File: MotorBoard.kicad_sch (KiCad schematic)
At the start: 34 parts

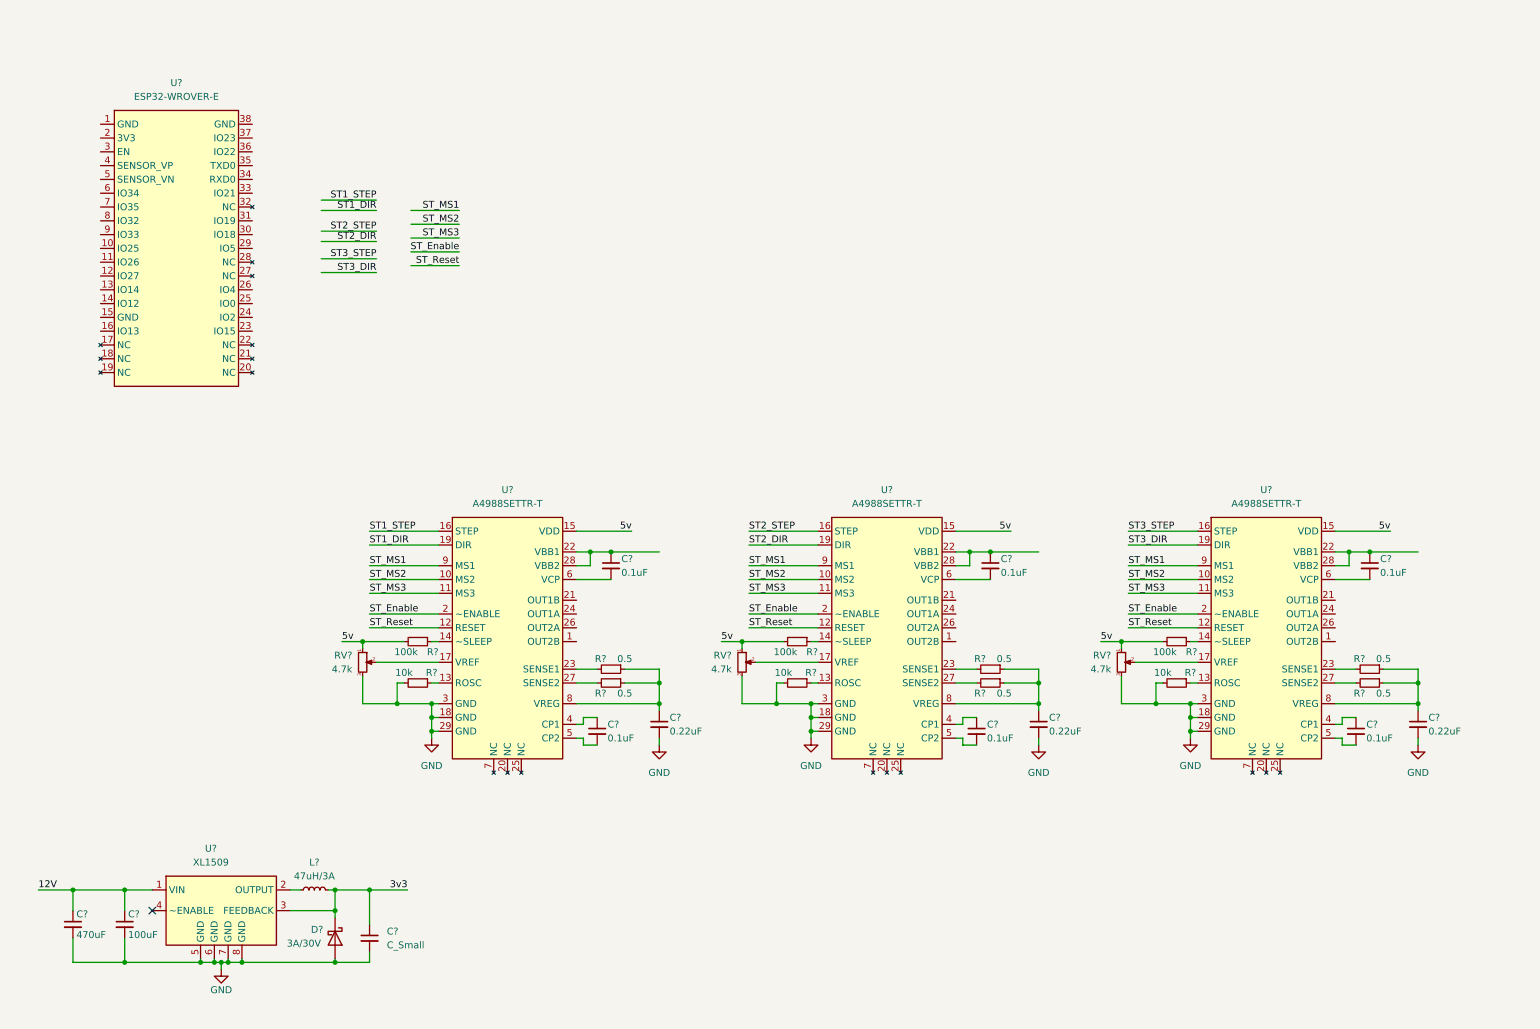
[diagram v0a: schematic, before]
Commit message: Wired stepper driver and power supply section
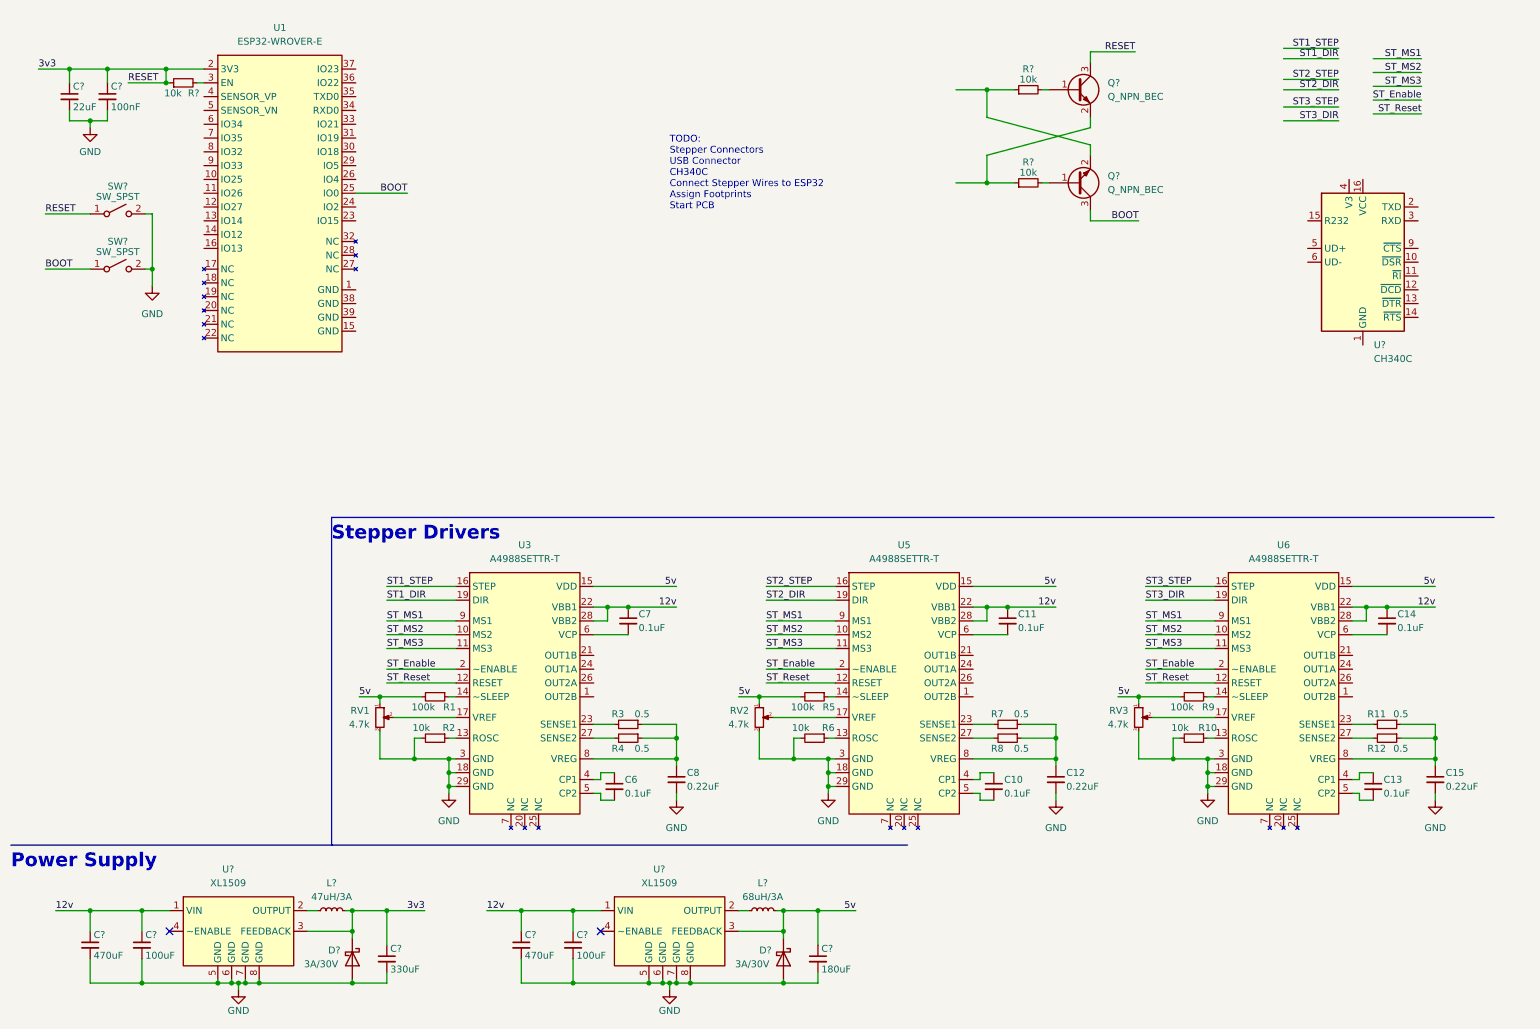
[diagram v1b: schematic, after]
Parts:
- removed C?: C_Small, symbol Device:C_Small
- removed C?: 100uF, symbol Device:C_Small
- removed C?: 470uF, symbol Device:C_Small
- removed D?: 3A/30V, symbol Device:D_Schottky
- removed L?: 47uH/3A, symbol Device:L_Small
- removed U?: XL1509, symbol MotorBoard:XL1509
- added C? (x2): 100uF, symbol Device:C_Small
- added C? (x2): 470uF, symbol Device:C_Small
- added C?: 330uF, symbol Device:C_Small
- added C?: 180uF, symbol Device:C_Small
- added C?: 100nF, symbol Device:C_Small
- added C?: 22uF, symbol Device:C_Small
- added D? (x2): 3A/30V, symbol Device:D_Schottky
- added L?: 47uH/3A, symbol Device:L_Small
- added L?: 68uH/3A, symbol Device:L_Small
- added Q? (x2): Q_NPN_BEC, symbol Device:Q_NPN_BEC
- added R? (x3): 10k, symbol Device:R_Small
- added SW? (x2): SW_SPST, symbol Switch:SW_SPST
- added U?: CH340C, Package_SO:SOIC-16_3.9x9.9mm_P1.27mm, symbol Interface_USB:CH340C
- added U? (x2): XL1509, symbol MotorBoard:XL1509
- U1: renamed from U?; LSCS Part Number (none) -> C2934565
- U3, U5, U6: renamed from U?; LSCS Part Number (none) -> C38437
- gave numbers to parts that had none: 24
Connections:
- net 3v3: now also U1.2 (3V3), C?.1, C?.1, C?.1, D?.1 (K), L?.2, Q?.3 (C), R?.1, SW?.1 (A), U?.3 (FEEDBACK)
- net 5v: now also C?.1, D?.1 (K), L?.2, U?.3 (FEEDBACK)
- net GND: now also C?.2, C?.2, C?.2, C?.2, C?.2, C?.2, C?.2, C?.2, D?.2 (A), D?.2 (A), SW?.2 (B), SW?.2 (B), U?.5 (GND), U?.5 (GND), U?.6 (GND), U?.6 (GND), U?.7 (GND), U?.7 (GND), U?.8 (GND), U?.8 (GND)
- net 12v: now reaches C14.1, U6.22 (VBB1), U6.28 (VBB2)
- net 12v: now also C11.1, C7.1, U3.22 (VBB1), U3.28 (VBB2), U5.22 (VBB1), U5.28 (VBB2), C?.1, C?.1, C?.1, C?.1, U?.1 (VIN), U?.1 (VIN)
- net BOOT: now reaches U1.25 (IO0)
- net BOOT: now also Q?.3 (C), SW?.1 (A)
- net at U1.3 (EN): now also R?.2
- new net: L?.1, U?.2 (OUTPUT) (x2)
- new net: Q?.1 (B), R?.2 (x2)
- new net: Q?.2 (E), R?.1 (x2)
- no-connect marks 1 -> 2
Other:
- note added: "Power Supply"
- note added: "Stepper Drivers"
- note added: "TODO: Stepper Connectors USB Connector CH340C Connect Stepper Wires to ESP32 Assign Footprints Start PCB"
- moved on the sheet: C10, C11, C12, C13, C14, C15, C6, C7, C8, R1, R10, R11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

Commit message: Broke stepper drivers into hierarchial sheets
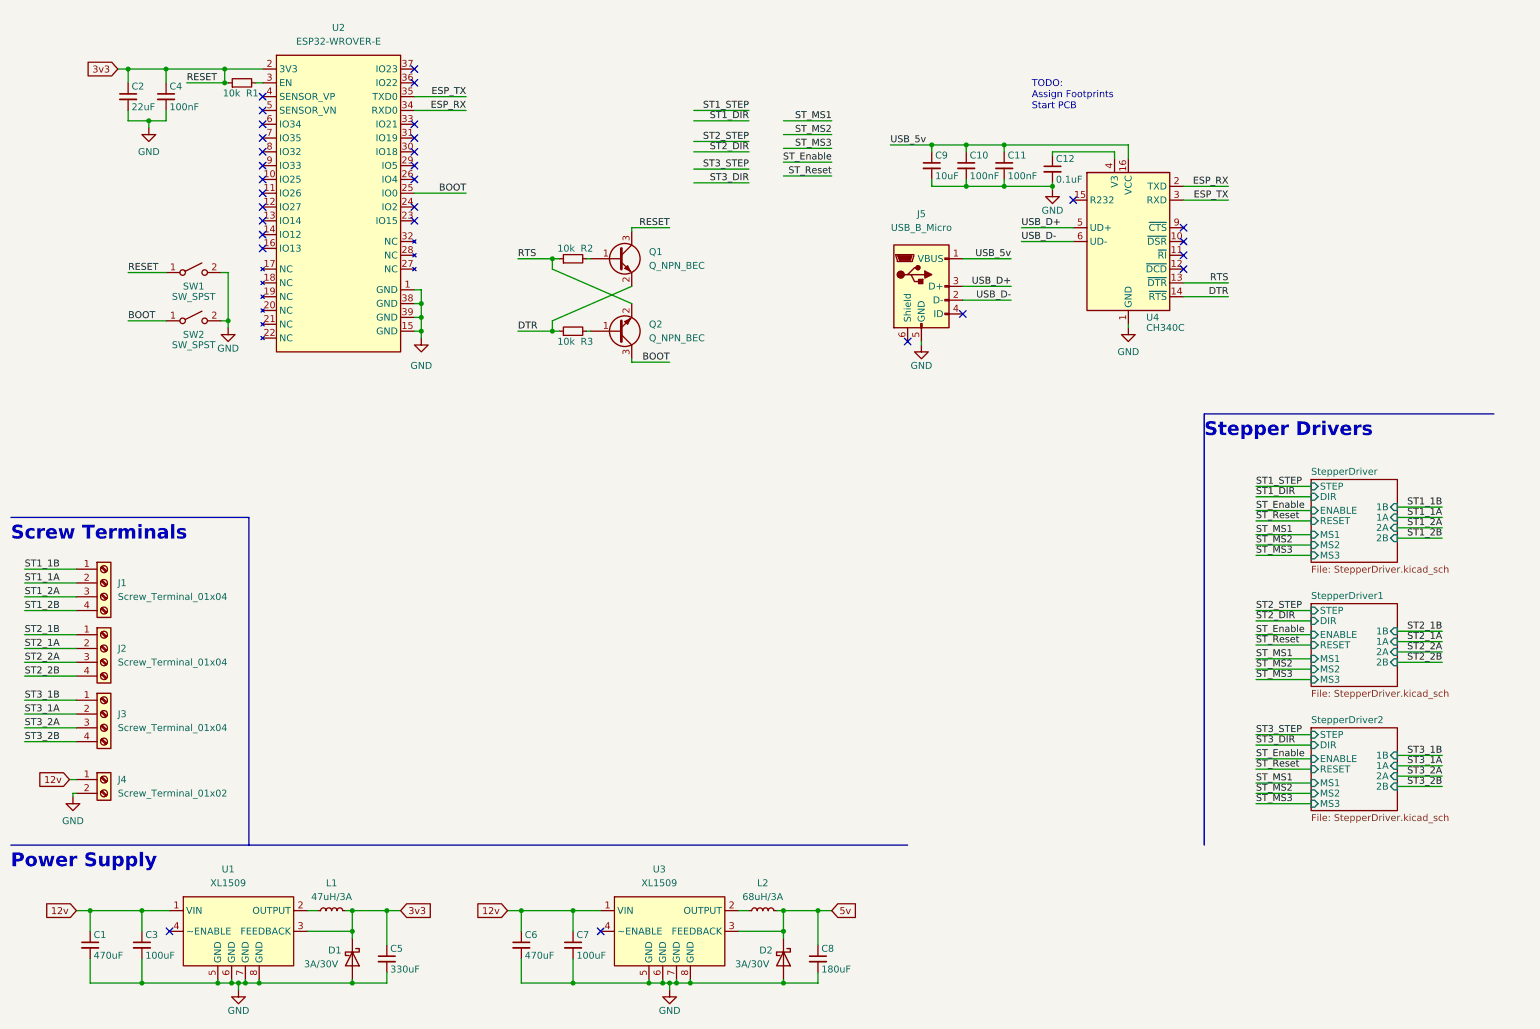
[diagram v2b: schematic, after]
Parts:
- removed C13, C14, C6, C7: 0.1uF, symbol Device:C_Small
- removed C15, C8: 0.22uF, symbol Device:C_Small
- removed R1, R5, R9: 100k, symbol Device:R_Small
- removed R10, R2, R6: 10k, symbol Device:R_Small
- removed R11, R12, R3, R4, R7, R8: 0.5, symbol Device:R_Small
- removed RV1, RV2, RV3: 4.7k, symbol Device:R_Potentiometer_Small
- removed U3, U5, U6: A4988SETTR-T, symbol MotorBoard:A4988SETTR-T
- added C9: 10uF, symbol Device:C_Small
- added J1, J2, J3: Screw_Terminal_01x04, symbol Connector:Screw_Terminal_01x04
- added J4: Screw_Terminal_01x02, symbol Connector:Screw_Terminal_01x02
- added J5: USB_B_Micro, symbol Connector:USB_B_Micro
- C10, C11: value 0.1uF -> 100nF
- C12: value 0.22uF -> 0.1uF
- gave numbers to parts that had none: 22
- renumbered U1 to U2
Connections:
- net 12v: now also J4.1 (Pin_1); no longer C11.1
- net GND: now also C10.2, C11.2, U2.1 (GND), U2.15 (GND), U2.38 (GND), U2.39 (GND), U4.1 (GND), C9.2, J4.2 (Pin_2), J5.5 (GND)
- net RTS: now reaches U4.13 (~{DTR})
- net RTS: now also Q2.2 (E), R2.1
- net DTR: now reaches U4.14 (~{RTS})
- net DTR: now also Q1.2 (E), R3.1
- net USB_5v: now reaches U4.16 (VCC)
- net USB_5v: now also C10.1, C11.1, C9.1, J5.1 (VBUS)
- net ESP_RX: now reaches U4.2 (TXD)
- net ESP_RX: now also U2.34 (RXD0)
- net ESP_TX: now reaches U4.3 (RXD)
- net ESP_TX: now also U2.35 (TXD0)
- net at U4.4 (V3): now also C12.1
- net USB_D+: now reaches U4.5 (UD+)
- net USB_D+: now also J5.3 (D+)
- net USB_D-: now reaches U4.6 (UD-)
- net USB_D-: now also J5.2 (D-)
- new net ST1_1A: J1.2 (Pin_2)
- new net ST1_1B: J1.1 (Pin_1)
- new net ST1_2A: J1.3 (Pin_3)
- new net ST1_2B: J1.4 (Pin_4)
- new net ST2_1A: J2.2 (Pin_2)
- new net ST2_1B: J2.1 (Pin_1)
- new net ST2_2A: J2.3 (Pin_3)
- new net ST2_2B: J2.4 (Pin_4)
- new net ST3_1A: J3.2 (Pin_2)
- new net ST3_1B: J3.1 (Pin_1)
- new net ST3_2A: J3.3 (Pin_3)
- new net ST3_2B: J3.4 (Pin_4)
- no-connect marks 2 -> 30
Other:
- added sheet StepperDriver (StepperDriver.kicad_sch)
- added sheet StepperDriver1 (StepperDriver.kicad_sch)
- added sheet StepperDriver2 (StepperDriver.kicad_sch)
- note added: "Screw Terminals"
- note added: "TODO: Assign Footprints Start PCB"
- note removed: "TODO: Stepper Connectors USB Connector CH340C Connect Stepper Wires to ESP32 Assign Footprints Start PCB"
- moved on the sheet: C2, C4, Q1, Q2, R1, R2, R3, SW1, SW2, U2, U4

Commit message: Added part numbers to majority of components
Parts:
- C1, C3, C5, C6, C7, C8: footprint (none) -> Capacitor_SMD:C_0603_1608Metric
- C10, C11, C4: footprint (none) -> Capacitor_SMD:C_0603_1608Metric; LSCS Part Number (none) -> C1591; Manufacturer Part Number (none) -> CL10B104KB8NNNC
- C12: value 0.1uF -> 100nF; footprint (none) -> Capacitor_SMD:C_0603_1608Metric; LSCS Part Number (none) -> C1591; Manufacturer Part Number (none) -> CL10B104KB8NNNC
- C2: footprint (none) -> Capacitor_SMD:C_0603_1608Metric; LSCS Part Number (none) -> C59461; Manufacturer Part Number (none) -> CL10A226MQ8NRNC
- C9: footprint (none) -> Capacitor_SMD:C_0603_1608Metric; LSCS Part Number (none) -> C19702; Manufacturer Part Number (none) -> CL10A106KP8NNNC
- D1, D2: footprint (none) -> Diode_SMD:D_SMA; LSCS Part Number (none) -> C8678; Manufacturer Part Number (none) -> SS34
- J1, J2, J3: LSCS Part Number (none) -> C393015; Manufacturer Part Number (none) -> JL124D-38104G01
- J4: LSCS Part Number (none) -> C474881; Manufacturer Part Number (none) -> KF301-5.0-2P
- J5: LSCS Part Number (none) -> C319160; Manufacturer Part Number (none) -> U254-051T-4BH83-S1S
- Q1, Q2: Manufacturer Part Number (none) -> PMBT3904,215
- R1, R2, R3: footprint (none) -> Resistor_SMD:R_0603_1608Metric; LSCS Part Number (none) -> C25804; Manufacturer Part Number (none) -> 0603WAF1002T5E
- SW1, SW2: LSCS Part Number (none) -> C318938; Manufacturer Part Number (none) -> TS-1101-C-W
- U1: Info (none) -> 3.3v; Manufacturer Part Number (none) -> XL1509-3.3
- U2: Manufacturer Part Number (none) -> ESP32-WROVER-IE(8MB)
- U3: Info (none) -> 5v; LSCS Part Number C2681226 -> C2902368; Manufacturer Part Number (none) -> XL1509-5.0
- U4: LSCS Part Number (none) -> C84681; Manufacturer Part Number (none) -> CH340C

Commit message: Started assigning footprints
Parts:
- removed D1, D2: 3A/30V, Diode_SMD:D_SMA, symbol Device:D_Schottky
- removed U1, U3: XL1509, symbol MotorBoard:XL1509
- added C10: 100uF, Capacitor_SMD:C_1210_3225Metric, symbol Device:C_Small
- added C9: 10uF, Capacitor_SMD:C_0603_1608Metric, symbol Device:C_Small
- added D1, D2: 1N5819, Diode_SMD:D_SOD-123, symbol Diode:1N5819
- added L3: 47uH, Inductor_SMD:L_Bourns-SRN8040_8x8.15mm, symbol Device:L_Small
- added L4: 1uH, Inductor_SMD:L_0603_1608Metric, symbol Device:L_Small
- added R1: 0.39, Resistor_SMD:R_0603_1608Metric, symbol Device:R_Small
- added R3: 18k, Resistor_SMD:R_0603_1608Metric, symbol Device:R_Small
- added R4: 11k, Resistor_SMD:R_0603_1608Metric, symbol Device:R_Small
- added R7: 0.5, Resistor_SMD:R_0603_1608Metric, symbol Device:R_Small
- added R8: 3k, Resistor_SMD:R_0603_1608Metric, symbol Device:R_Small
- added R9: 1k, Resistor_SMD:R_0603_1608Metric, symbol Device:R_Small
- added U1, U3: MC34063AD, Package_SO:SOP-8_3.9x4.9mm_P1.27mm, symbol Regulator_Switching:MC34063AD
- C1, C6: value 470uF -> 100uF; footprint Capacitor_SMD:C_0603_1608Metric -> Capacitor_SMD:C_1210_3225Metric; LSCS Part Number (none) -> C90143; Manufacturer Part Number (none) -> EMK325ABJ107MM-P
- C3: value 100uF -> 150pF; LSCS Part Number (none) -> C1594; Manufacturer Part Number (none) -> 0603B151K500NT
- C5: value 330uF -> 10uF; LSCS Part Number (none) -> C19702; Manufacturer Part Number (none) -> CL10A106KP8NNNC
- C7: footprint Capacitor_SMD:C_0603_1608Metric -> Capacitor_SMD:C_1210_3225Metric; LSCS Part Number (none) -> C90143; Manufacturer Part Number (none) -> EMK325ABJ107MM-P
- C8: value 180uF -> 200pF; LSCS Part Number (none) -> C1649; Manufacturer Part Number (none) -> 0603CG201J500NT
- J1, J2, J3: footprint (none) -> TerminalBlock:TerminalBlock_Altech_AK300-4_P5.00mm
- J4: footprint (none) -> TerminalBlock:TerminalBlock_Altech_AK300-2_P5.00mm
- J5: footprint (none) -> MotorBoard:U254-051T-4BH83-S1S
- L1: value 47uH/3A -> 33uH; footprint (none) -> Inductor_SMD:L_Bourns-SRN6028; LSCS Part Number (none) -> C2929433; Manufacturer Part Number (none) -> CY54-33UH
- L2: value 68uH/3A -> 1uH; footprint (none) -> Inductor_SMD:L_0603_1608Metric; LSCS Part Number (none) -> C383366; Manufacturer Part Number (none) -> MLP1608V1R0BT0S1
- Q1, Q2: footprint (none) -> Package_TO_SOT_SMD:SOT-23
- U2: footprint (none) -> MotorBoard:ESP32-WROVER-IE
- renumbered C9 to C11, C10 to C12, C11 to C13, C12 to C14, R1 to R2, R2 to R5, R3 to R6
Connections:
- net 12v: now also R1.1, R7.1, U1.6 (Vin), U3.6 (Vin); no longer C3.1, C6.1
- net 3v3: now also C6.1, L2.2; no longer C5.1, L1.2
- net 5v: now also C10.1, L4.2; no longer C8.1, L2.2
- net GND: now also C10.2, C9.2, D1.2 (A), D2.2 (A), R4.2, R9.2, U1.4 (GND), U3.4 (GND)
- net at L1.1: now also D1.1 (K), U1.2 (SwE)
- net at L2.1: now also C5.1, L1.2, R3.1
- new net: C9.1, L3.2, L4.1, R8.1
- new net: D2.1 (K), L3.1, U3.2 (SwE)
- new net: C3.1, U1.3 (TC)
- new net: R8.2, R9.1, U3.5 (Vfb)
- new net: R7.2, U3.1 (SwC), U3.7 (Ipk), U3.8 (DC)
- new net: C8.1, U3.3 (TC)
- new net: R3.2, R4.1, U1.5 (Vfb)
- new net: R1.2, U1.1 (SwC), U1.7 (Ipk), U1.8 (DC)
- no-connect marks 30 -> 28
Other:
- note added: "Design Parameters: 12v In, 3.3v Out 400mA Output Current 100mV Ripple 100kHz Frequency"
- note added: "Design Parameters: 12v In, 5v Out 300mA Output Current 100mV Ripple 100kHz Frequency"
- moved on the sheet: J1, J2, J3, J4
